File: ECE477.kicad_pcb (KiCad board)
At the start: 2 copper layers, 88.9 x 88.9 mm, 55 parts, among them IC1 LP3852EMP-3.3_NOPB, IC2 BQ29330DBT, J1 P7805-2000-S, J10 Conn_01x01_Male, J11 Conn_01x01_Male, J2 Conn_01x05_Male, J3 Conn_01x05_Male, J4 Conn_01x05_Male, J5 Conn_01x05_Male, J6 Conn_01x05_Male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

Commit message: DRC corrections
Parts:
- moved J1 1.80 mm to (238.8, 69.8)
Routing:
- net GND: track 689.0 -> 691.6 mm
- net Net-(C35-Pad1): track 12.3 -> 14.1 mm
- net 5V: track 63.4 -> 64.1 mm

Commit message: Board label
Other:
- board text added: "ECE 477 Team 4 / Rev 1 completed 10-15-2020 Josh Panos - Moiz Rasheed / Ethan Campbell - Jackie Malayter"

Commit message: naming
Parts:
- J10: value Conn_01x01_Male -> USART3
- J11: value Conn_01x01_Male -> USART1
- J9: value Conn_01x01_Male -> USART6

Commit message: Major change
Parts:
- removed IC2: BQ29330DBT, SamacSys_Parts:SOP50P640X120-30N
- added C10: 1uF, Capacitor_SMD:C_0805_2012Metric_Pad1.15x1.40mm_HandSolder, B.Cu at (246.1, 83.8)
- added C2: 1uF, Capacitor_SMD:C_0805_2012Metric_Pad1.15x1.40mm_HandSolder, B.Cu at (227.3, 81.0)
- added C3: 1uF, Capacitor_SMD:C_0805_2012Metric_Pad1.15x1.40mm_HandSolder, F.Cu at (227.3, 84.8)
- added C4: 1uF, Capacitor_SMD:C_0805_2012Metric_Pad1.15x1.40mm_HandSolder, B.Cu at (229.9, 87.6)
- added C5: 1uF, Capacitor_SMD:C_0805_2012Metric_Pad1.15x1.40mm_HandSolder, F.Cu at (227.3, 90.2)
- added C6: 1uF, Capacitor_SMD:C_0805_2012Metric_Pad1.15x1.40mm_HandSolder, B.Cu at (229.9, 93.0)
- added C7: 10uF, Capacitor_THT:CP_Radial_D5.0mm_P2.50mm, F.Cu at (243.8, 78.7)
- added C8: 1uF, Capacitor_SMD:C_0805_2012Metric_Pad1.15x1.40mm_HandSolder, B.Cu at (246.4, 86.4)
- added C9: 1uF, Capacitor_SMD:C_0805_2012Metric_Pad1.15x1.40mm_HandSolder, F.Cu at (236.2, 81.0)
- added IC3: BQ7692006PWR, SamacSys_Parts:SOP65P640X120-20N, F.Cu at (239.2, 86.7)
- added R15: 100, Resistor_SMD:R_0805_2012Metric_Pad1.15x1.40mm_HandSolder, B.Cu at (223.3, 80.0)
- added R16: 100, Resistor_SMD:R_0805_2012Metric_Pad1.15x1.40mm_HandSolder, B.Cu at (223.3, 86.4)
- added R17: 100, Resistor_SMD:R_0805_2012Metric_Pad1.15x1.40mm_HandSolder, F.Cu at (223.3, 88.9)
- added R18: 100, Resistor_SMD:R_0805_2012Metric_Pad1.15x1.40mm_HandSolder, B.Cu at (223.5, 91.4)
- added R19: 1k, Resistor_SMD:R_0805_2012Metric_Pad1.15x1.40mm_HandSolder, F.Cu at (218.4, 98.8)
- added R20: 0R, Resistor_SMD:R_0805_2012Metric_Pad1.15x1.40mm_HandSolder, F.Cu at (230.1, 96.5)
- added R21: 1k, Resistor_SMD:R_0805_2012Metric_Pad1.15x1.40mm_HandSolder, F.Cu at (223.5, 99.1)
- added R22: 0R, Resistor_SMD:R_0805_2012Metric_Pad1.15x1.40mm_HandSolder, F.Cu at (235.2, 99.1)
- added R23: 100, Resistor_SMD:R_0805_2012Metric_Pad1.15x1.40mm_HandSolder, F.Cu at (238.8, 78.7)
- added R24: 0R, Resistor_SMD:R_0805_2012Metric_Pad1.15x1.40mm_HandSolder, B.Cu at (239.8, 82.5)
- added R25: 0R, Resistor_SMD:R_0805_2012Metric_Pad1.15x1.40mm_HandSolder, B.Cu at (236.2, 94.0)
- added R26: 1M, Resistor_SMD:R_0805_2012Metric_Pad1.15x1.40mm_HandSolder, B.Cu at (237.5, 114.1)
- added R9: 100, Resistor_SMD:R_0805_2012Metric_Pad1.15x1.40mm_HandSolder, F.Cu at (223.3, 83.8)
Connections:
- U1 pad 21: CLK -> Net-(U1-Pad21)
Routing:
- net CLK: track 74.3 -> 0.00 mm, vias 2 -> 0
- net GND: track 691.6 -> 752.4 mm, vias 22 -> 24
- net I2C2_SMBA: track 41.8 -> 0.00 mm, vias 2 -> 0
- net PIN1: track 24.9 -> 50.9 mm
- net CELL-: track 24.1 -> 0.00 mm
- net CELL+: track 20.4 -> 0.00 mm
- net SDA_1: track 0.00 -> 19.0 mm
- net cell_3: track 0.00 -> 18.5 mm, vias 0 -> 1
- net SCL_1: track 0.00 -> 17.7 mm
- net I2C2_SDA: track 41.6 -> 23.9 mm, vias 2 -> 0
- net cell_2: track 0.00 -> 17.4 mm, vias 0 -> 1
- net cell_1: track 0.00 -> 15.5 mm, vias 0 -> 1
- net I2C2_SCL: track 41.1 -> 26.1 mm
- net cell_pwr: track 0.00 -> 14.1 mm, vias 0 -> 1
- net VDD_MCU: track 489.0 -> 503.0 mm, vias 4 -> 6
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
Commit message: PE9
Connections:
- R25 pad 2: PIN1 -> PIN2
- R26 pad 1: PIN1 -> PIN2
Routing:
- net PIN2: track 24.1 -> 50.0 mm
- net PIN1: track 50.9 -> 24.9 mm
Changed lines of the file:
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@@
     (thickness 1.6)
     (drawings 14)
-    (tracks 855)
+    (tracks 856)
     (zones 0)
     (modules 77)
@@
       (net 1 GND))
     (pad 1 smd roundrect (at -1.025 0 270) (size 1.15 1.4) (layers B.Cu B.Paste B.Mask) (roundrect_rratio 0.217391)
-      (net 121 PIN1))
+      (net 122 PIN2))
     (model ${KISYS3DMOD}/Resistor_SMD.3dshapes/R_0805_2012Metric.wrl
       (at (xyz 0 0 0))
@@
     (fp_line (start 1.85 -0.95) (end -1.85 -0.95) (layer B.CrtYd) (width 0.05))
     (pad 2 smd roundrect (at 1.025 0 270) (size 1.15 1.4) (layers B.Cu B.Paste B.Mask) (roundrect_rratio 0.217391)
-      (net 121 PIN1))
+      (net 122 PIN2))
     (pad 1 smd roundrect (at -1.025 0 270) (size 1.15 1.4) (layers B.Cu B.Paste B.Mask) (roundrect_rratio 0.217391)
       (net 142 ALERT))
@@
   (segment (start 220.500001 104.930001) (end 229.87 114.3) (width 0.25) (layer F.Cu) (net 121))
   (segment (start 208.8388 104.930001) (end 220.500001 104.930001) (width 0.25) (layer F.Cu) (net 121))
-  (segment (start 236.22 111.76) (end 237.49 113.03) (width 0.25) (layer B.Cu) (net 121))
-  (segment (start 236.22 95.005) (end 236.22 111.76) (width 0.25) (layer B.Cu) (net 121))
-  (segment (start 232.41 111.76) (end 229.87 114.3) (width 0.25) (layer B.Cu) (net 121))
-  (segment (start 236.22 111.76) (end 232.41 111.76) (width 0.25) (layer B.Cu) (net 121))
   (segment (start 222.539999 104.429999) (end 229.87 111.76) (width 0.25) (layer F.Cu) (net 122))
   (segment (start 208.8388 104.429999) (end 222.539999 104.429999) (width 0.25) (layer F.Cu) (net 122))
+  (segment (start 236.22 111.76) (end 237.49 113.03) (width 0.25) (layer B.Cu) (net 122))
+  (segment (start 229.87 111.76) (end 233.68 111.76) (width 0.25) (layer B.Cu) (net 122))
+  (segment (start 233.68 111.76) (end 236.22 109.22) (width 0.25) (layer B.Cu) (net 122))
+  (segment (start 236.22 95.005) (end 236.22 109.22) (width 0.25) (layer B.Cu) (net 122))
+  (segment (start 236.22 109.22) (end 236.22 111.76) (width 0.25) (layer B.Cu) (net 122))
   (segment (start 224.58 103.93) (end 229.87 109.22) (width 0.25) (layer F.Cu) (net 123))
   (segment (start 208.8388 103.93) (end 224.58 103.93) (width 0.25) (layer F.Cu) (net 123))

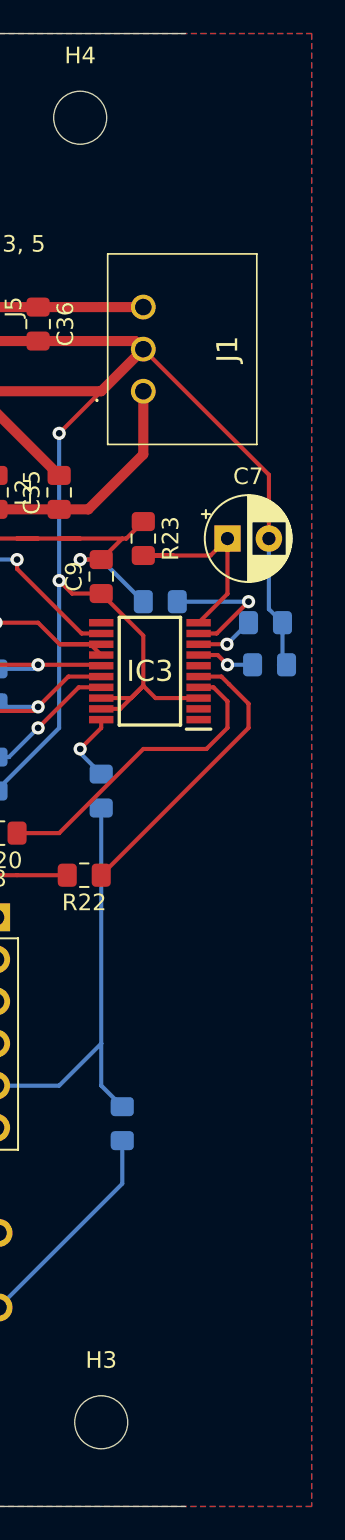
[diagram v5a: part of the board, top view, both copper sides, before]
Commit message: Updated layout
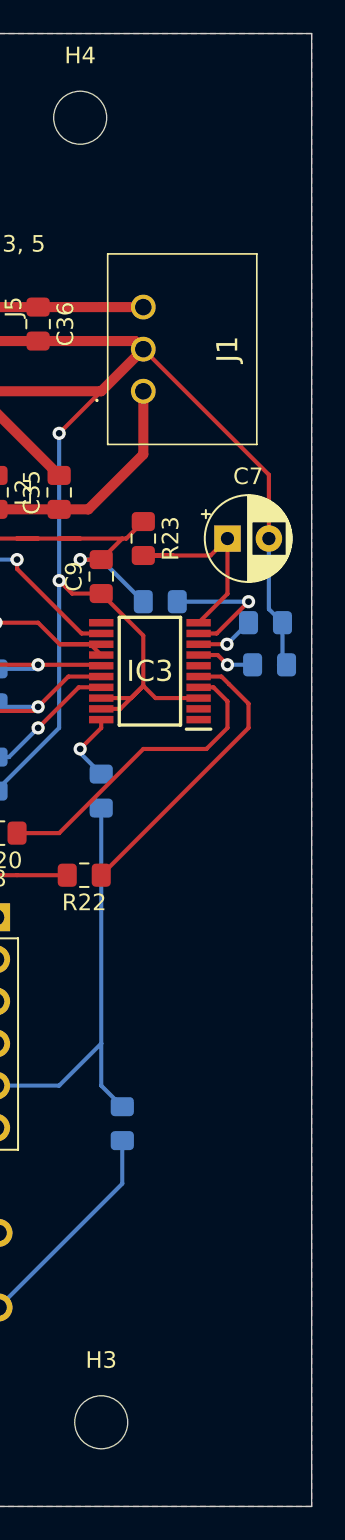
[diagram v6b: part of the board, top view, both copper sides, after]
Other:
- board size 88.9 x 88.9 mm -> 96.5 x 88.9 mm
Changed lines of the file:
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@@
   (general
     (thickness 1.6)
-    (drawings 14)
+    (drawings 17)
     (tracks 856)
     (zones 0)
@@
     )
   )
+  (gr_line (start 248.92 137.16) (end 241.3 137.16) (layer Edge.Cuts) (width 0.05))
+  (gr_line (start 248.92 48.26) (end 248.92 137.16) (layer Edge.Cuts) (width 0.05))
+  (gr_line (start 241.3 48.26) (end 248.92 48.26) (layer Edge.Cuts) (width 0.05))
   (gr_text "ECE 477 Team 4 / Rev 1 completed 10-15-2020\nJosh Panos - Moiz Rasheed \n/\nEthan Campbell - Jackie Malayter" (at 207.01 52.07) (layer F.SilkS)
     (effects (font (size 1 1) (thickness 0.15)))

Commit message: Updated
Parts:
- added R27: 10k, Resistor_SMD:R_0805_2012Metric_Pad1.15x1.40mm_HandSolder, B.Cu at (238.8, 92.5)
- added R28: 10k, Resistor_SMD:R_0805_2012Metric_Pad1.15x1.40mm_HandSolder, B.Cu at (241.3, 93.0)
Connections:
- IC3 pad 6: Net-(IC3-Pad6) -> BOOT_IC
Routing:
- net BOOT_IC: track 0.00 -> 10.1 mm, vias 0 -> 1
- net cell_1: track 15.5 -> 23.8 mm
- net GND: track 752.4 -> 750.5 mm

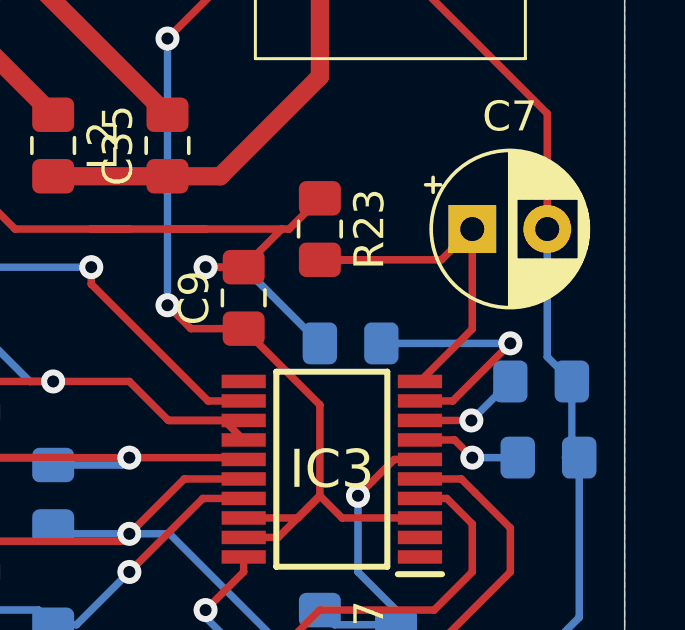
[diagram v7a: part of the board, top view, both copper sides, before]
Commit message: Fixed DRC issue
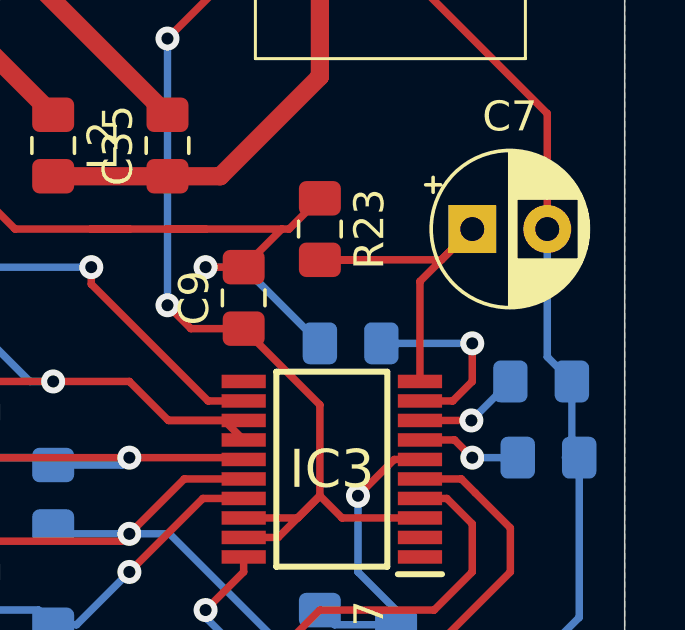
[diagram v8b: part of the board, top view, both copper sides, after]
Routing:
- net REGSRC: track 8.11 -> 6.31 mm
